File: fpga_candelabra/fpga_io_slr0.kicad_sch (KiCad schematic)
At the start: 1 part, among them U1 XCVU13P-B2104

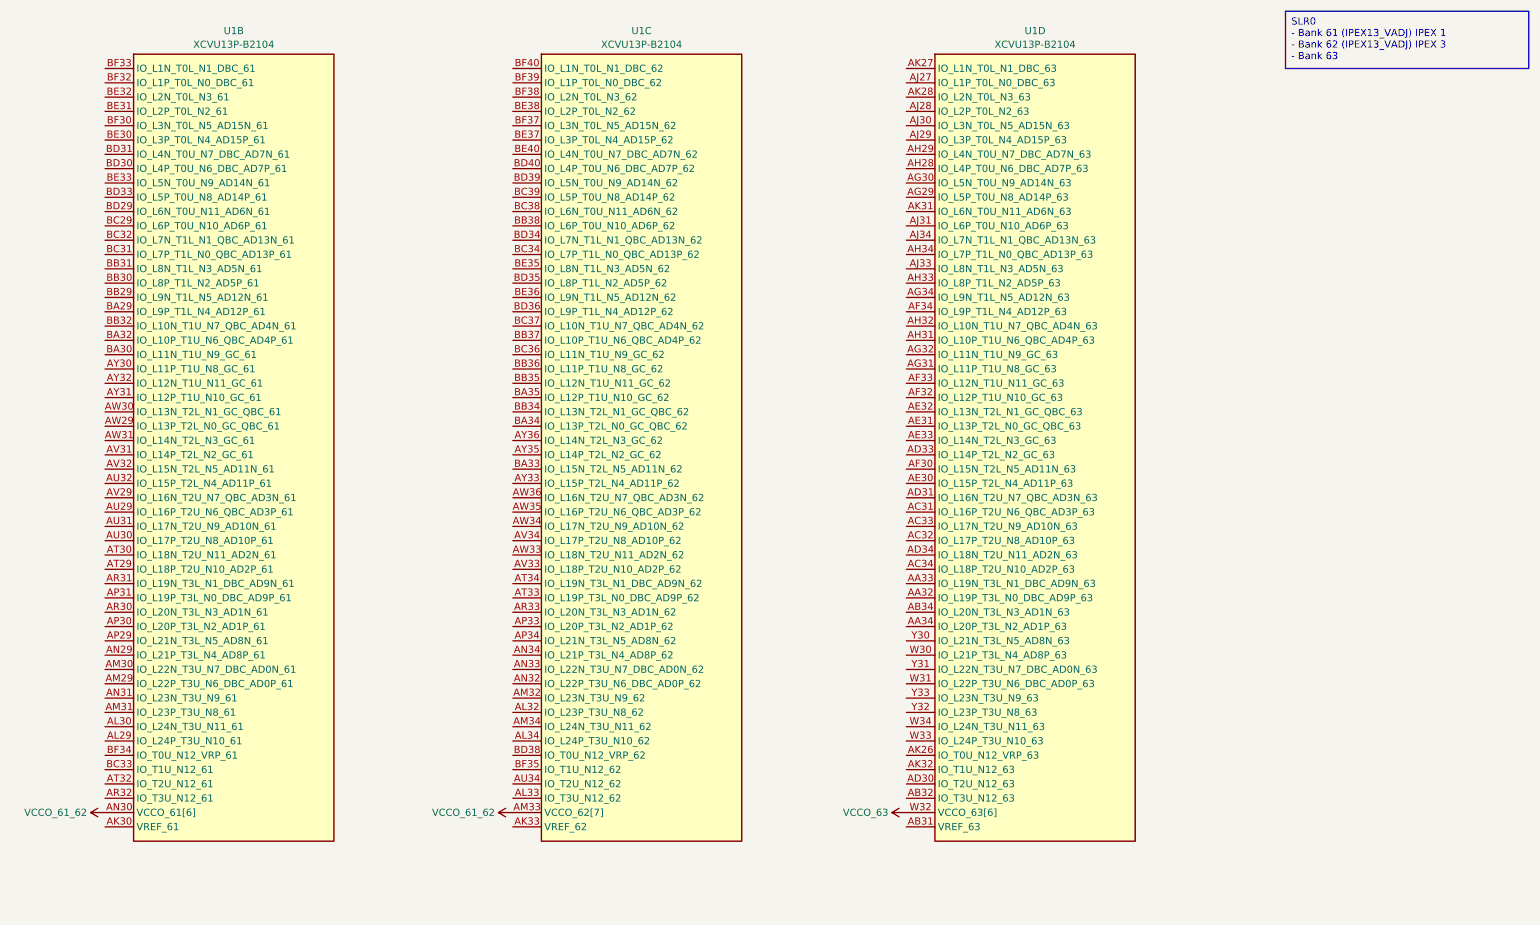
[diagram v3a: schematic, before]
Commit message: fpga_candelabra: sch & layout v0.5, pass basic ERC & DRC
Signed-off-by: Yichuan Gao <gaoyichuan000@gmail.com>
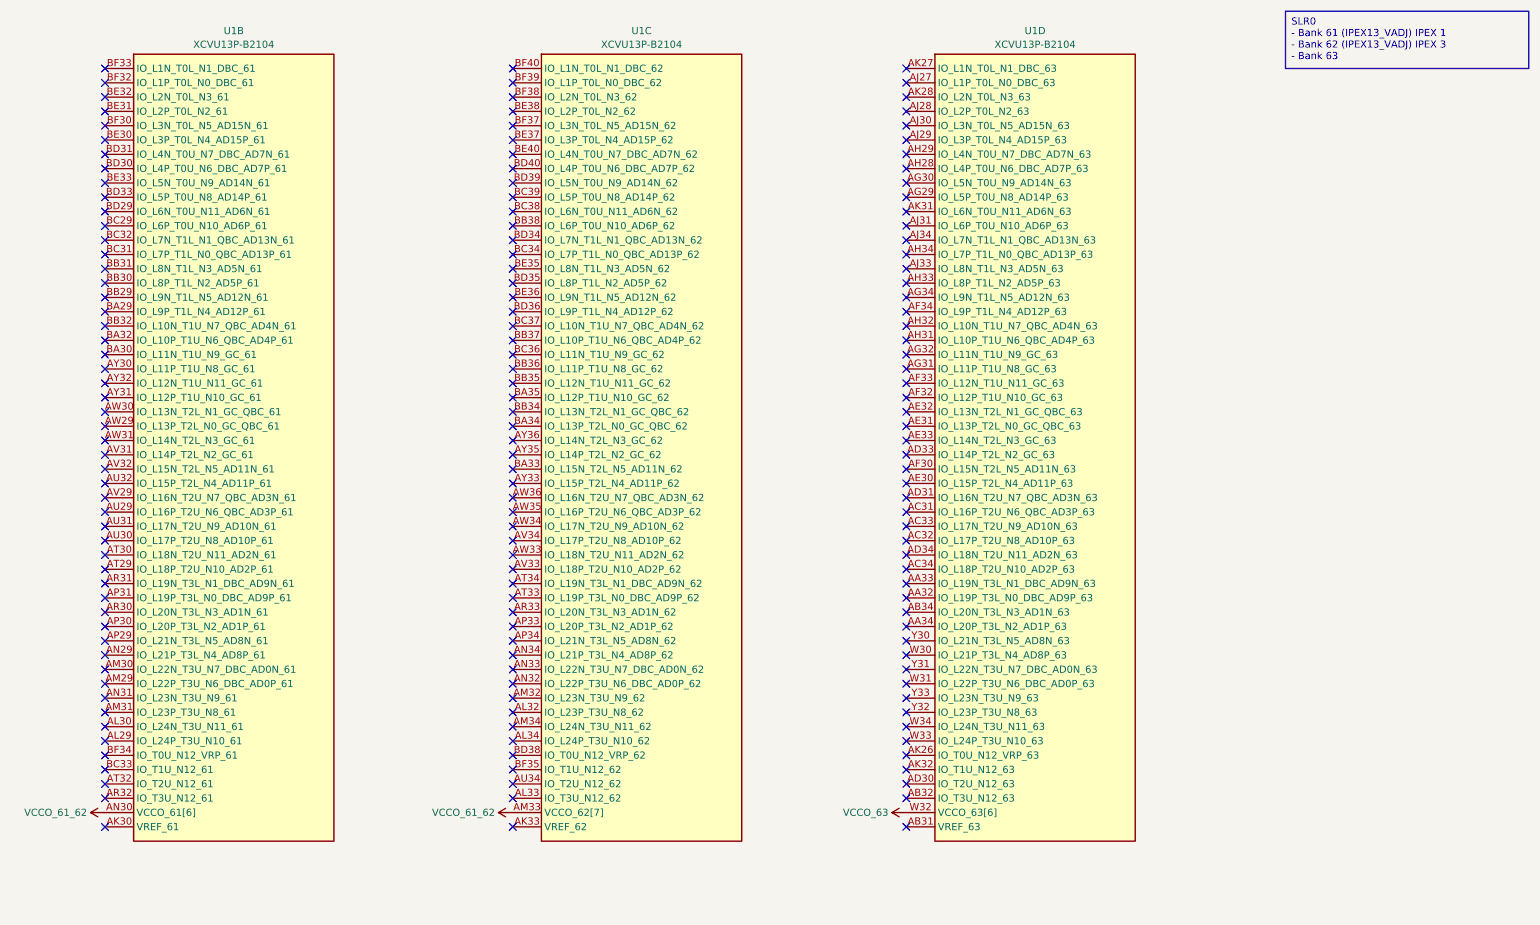
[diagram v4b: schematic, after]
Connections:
- no-connect marks 0 -> 159

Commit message: fpga_candelabra: add author & rev to schematics
Signed-off-by: Yichuan Gao <gaoyichuan000@gmail.com>
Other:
- company: (none) -> CHIPS Alliance
- title: (none) -> FPGA SLR0 IO
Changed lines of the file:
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@@
 	(generator_version "8.0")
 	(paper "A4")
+	(title_block
+		(title "FPGA SLR0 IO")
+		(date "2025-02-05")
+		(rev "0.2.0")
+		(company "CHIPS Alliance")
+		(comment 1 "Yichuan Gao")
+		(comment 2 "Yichuan Gao")
+	)
 	(no_connect
 		(at 30.48 105.41)

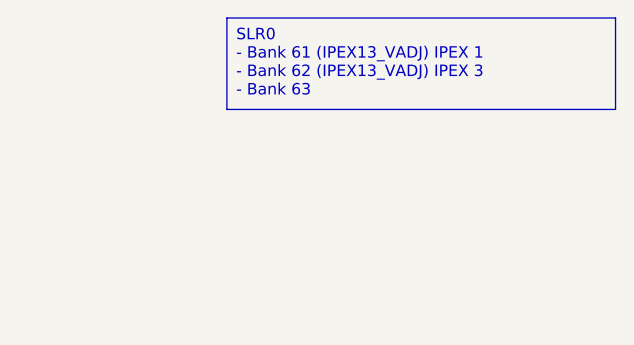
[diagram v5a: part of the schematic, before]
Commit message: fpga_candelabra: update to kicad 9.0
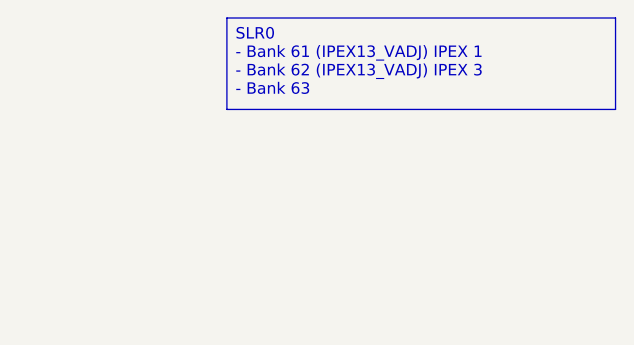
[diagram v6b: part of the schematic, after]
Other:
- company: CHIPS Alliance -> Sipeed
